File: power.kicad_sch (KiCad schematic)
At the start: 41 parts, among them T1 net-tie, U2 TPS546D24ARVFR

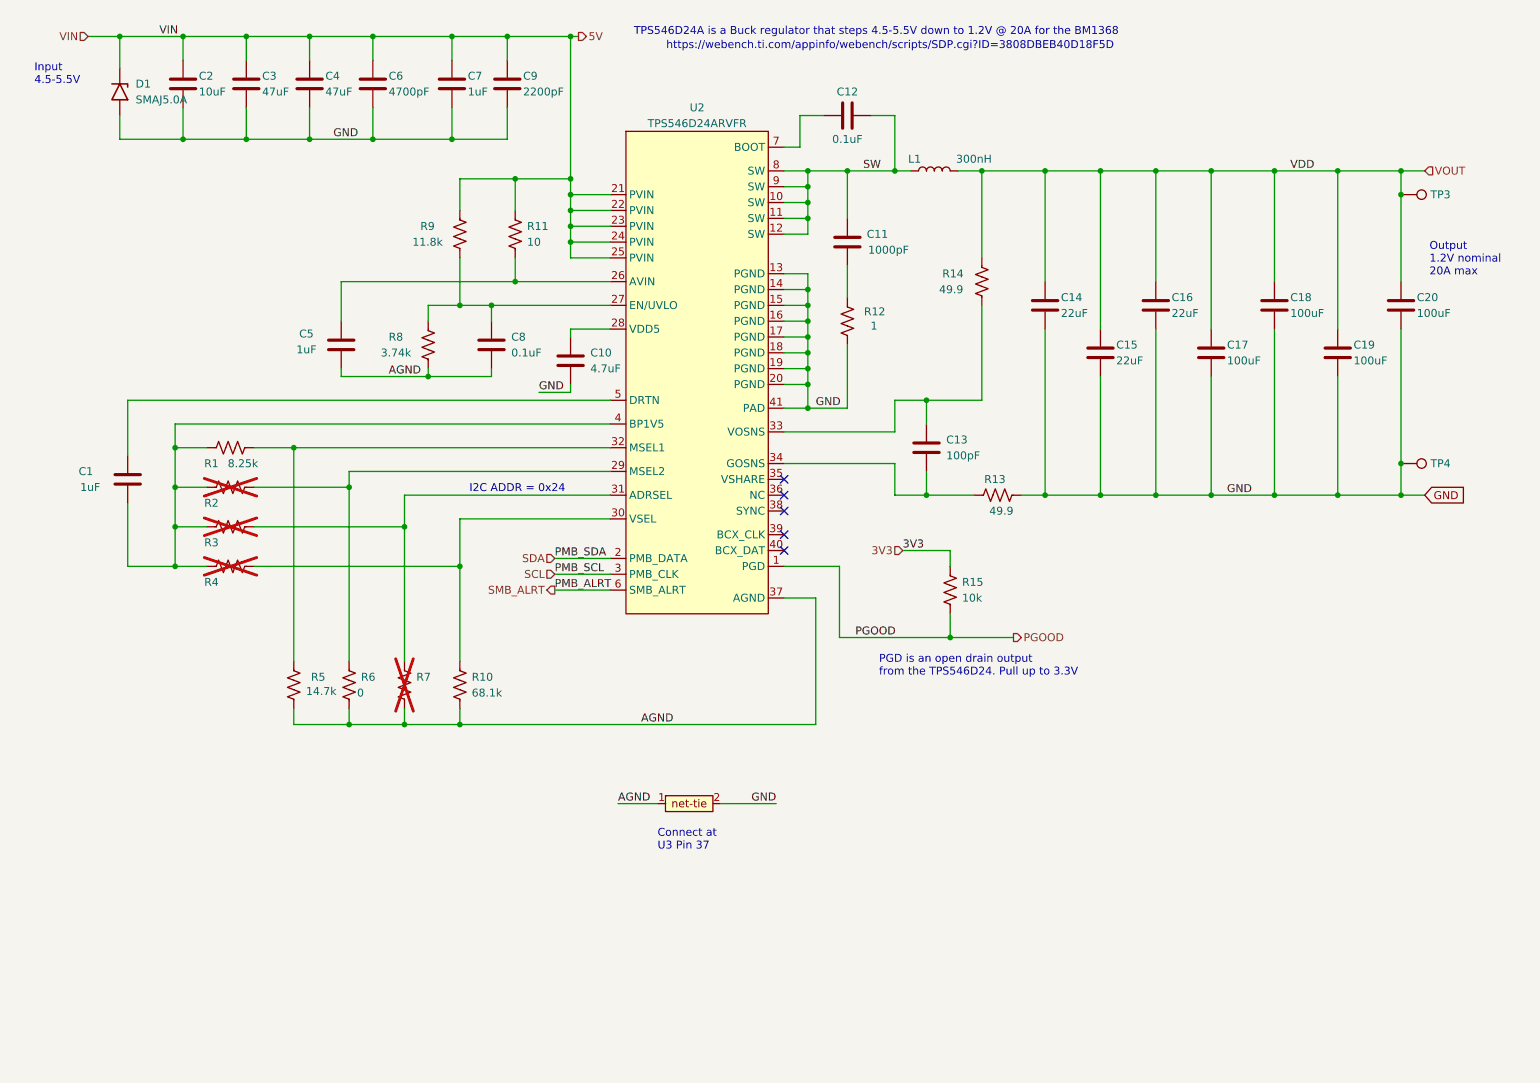
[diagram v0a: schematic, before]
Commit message: Nerdaxe Gamma v2.3
- Fix Emi CE needs
- Added ferrite beads + EMI blocking capacitors
- New components added: R16, R20, R26, R27C21, C22, C23, FB1, FB2, FB3, FB4, FB5, FB6
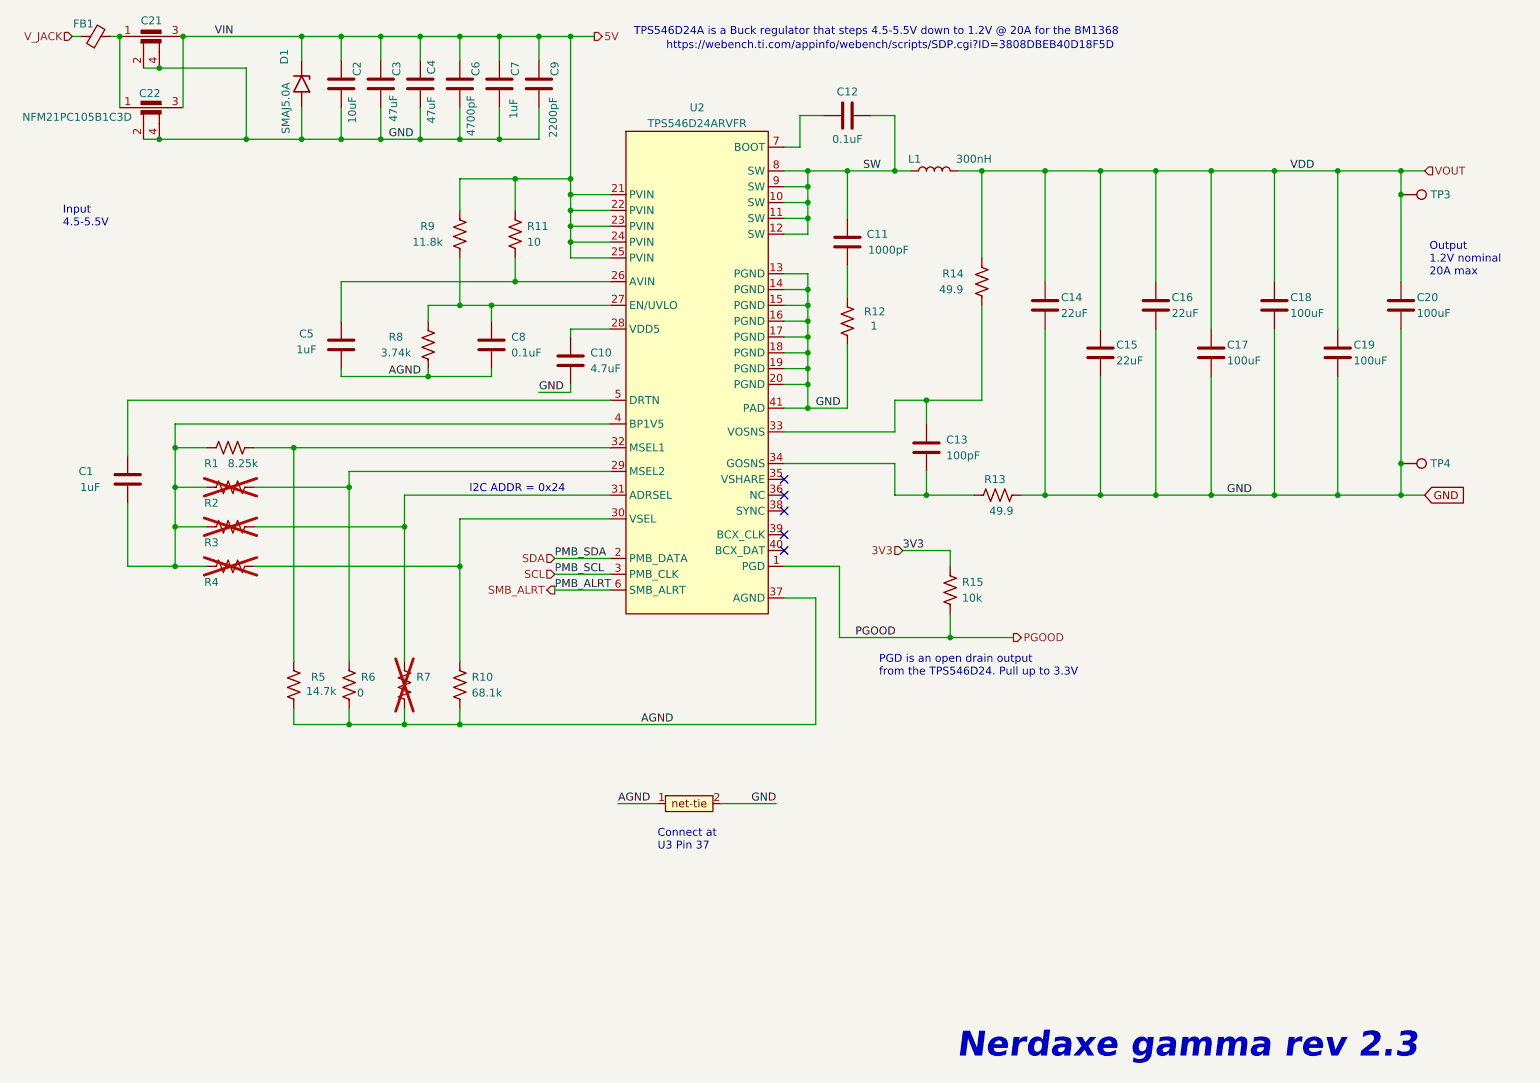
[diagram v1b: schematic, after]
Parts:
- added C21, C22: NFM21PC105B1C3D, bitaxe:NFM21PC105B1C3D_MUR, symbol Device:Filter_EMI_C
- added FB1: 2508051217Y6, Resistor_SMD:R_0805_2012Metric, symbol Device:FerriteBead_Small
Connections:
- net 5V: now also C21.3, C22.3
- net GND: now also C21.2, C21.4, C22.2, C22.4
- new net: C21.1, C22.1, FB1.2
- new net V_JACK: FB1.1
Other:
- note added: "Nerdaxe gamma rev 2.3"
- moved on the sheet: C2, C3, C4, C6, C7, C9, D1
